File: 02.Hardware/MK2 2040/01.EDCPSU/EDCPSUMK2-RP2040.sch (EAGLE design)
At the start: 192 parts, among them IC1 W25Q64JVSSIQ, IC2 LM4040C25FTA, IC3 AP64501SP-13, J1 DX07S016JA1R1500, J2 RP2040TR7, J4 FTDI CONECTOR, J6 Display, K1 FLEX CONNECTORES, Q2 2N7002PW, Q4 2N7002PW, Q5 2N7002PW, Q9 2N7002PW, U10 IP2721, U2 MCP4725, U3 SN74AC14PWR, U4 MAX9938FEUK+T, U6 SN74AC14PWR, U7 TPIC2810D, U9 MAX9064EUK+T, Y1 ABLS-12.000MHZ-B4-T

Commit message: correccion esquamtico
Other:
- note added: "3v3 DCDC Buck"
- note removed: "3v3 LDO/DCDC Buck"
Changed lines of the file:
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@@
 Fc= 7Hz</text>
 <text x="-474.98" y="198.12" size="6.4516" layer="94">SWD PROGRAMMER CONNECTOR</text>
-<text x="-462.28" y="106.68" size="6.4516" layer="94">3v3 LDO/DCDC Buck</text>
+<text x="-462.28" y="106.68" size="6.4516" layer="94">3v3 DCDC Buck</text>
 <text x="-439.42" y="86.36" size="1.778" layer="91">OJO:
 Indicar en BOM que

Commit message: 1º Colocacion de componentes en el brd
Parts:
- removed R38: N.C, SparkFun-Resistors:RESISTOR0805
- removed TP1, TP10, TP11, TP12, TP14, TP4, TP6, TP7, TP9: M01POGOPIN_HOLE_LARGE, SparkFun-Connectors:M01POGOPIN_HOLE_LARGE
- removed TP2: VCCIO, SparkFun-Connectors:M01POGOPIN_HOLE_LARGE
- removed TP3: M01NOSILK-KIT, SparkFun-Connectors:M01NOSILK-KIT
- removed TP5: PEDAL, SparkFun-Connectors:M01POGOPIN_HOLE_LARGE
- added C65: N.C., SparkFun-Passives:CAP0805
- added JP1, JP2, JP5: JUMPER-SMT_2_NO_NO-SILK, SparkFun-Jumpers:JUMPER-SMT_2_NO_NO-SILK
- added R58, R60: N.C, SparkFun-Resistors:RESISTOR0805
- C45, C46: device SparkFun-Passives:CAP1206 -> SparkFun-Passives:CAP0805
- Y1: value ABLS-12.000MHZ-B4-T -> ABM3C-12.000MHZ-D4Y-T; device ABLS-12.000MHZ-B4-T:ABLS-12.000MHZ-B4-T -> ABM3C-12.000MHZ-D4Y-T:ABM3C-12.000MHZ-D4Y-T
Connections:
- net SPARE renamed PDL
- removed net IN+1: D1.2
- removed net SPARE2: R38.1
- removed net VCC-ISO: C1.2, C12.2, C15.1, C16.2, C2.2, C20.2, C25.2, C26.1, C3.2, C31.2, C44.2, C45.1, C5.2, C50.2, C51.2, C52.2, C53.2, C57.1, C6.2, C60.2, C62.2, C7.2, C8.2, D2.C, D3.C, D7.C, IC1.VCC, J2.IOVDD_1, J2.IOVDD_2, J2.IOVDD_3, J2.IOVDD_4, J2.IOVDD_5, J2.IOVDD_6, J2.USB_VDD, J2.VREG_VIN, J4.VCC, J6.VCC, K1.P$4, L1.2, LS1.DUMMY, R13.2, R15.1, R19.2, R35.1, R40.2, R52.2, R53.2, R54.2, R57.2, R66.1, U2.VDD, U3P.VCC, U6P.VCC, U7.VCC, U9.VCC, Z1.K
- removed net VCCIO: TP2.1
- new net 3V3MCU: C1.2, C12.2, C15.1, C16.2, C2.2, C20.2, C25.2, C26.1, C3.2, C31.2, C44.2, C45.1, C5.2, C50.2, C51.2, C52.2, C53.2, C57.1, C6.2, C60.2, C62.2, C7.2, C8.2, D2.C, D3.C, D7.C, IC1.VCC, J2.IOVDD_1, J2.IOVDD_2, J2.IOVDD_3, J2.IOVDD_4, J2.IOVDD_5, J2.IOVDD_6, J2.USB_VDD, J2.VREG_VIN, J4.VCC, J6.VCC, K1.P$4, L1.2, LS1.+, R13.2, R15.1, R19.2, R35.1, R40.2, R52.2, R53.2, R54.2, R57.2, R66.1, U2.VDD, U3P.VCC, U6P.VCC, U7.VCC, U9.VCC, Z1.K
- new net N$45: R58.2, U2.SCL
- new net N$48: R60.2, U2.SDA
- net FB: now also JP2.2; no longer C52.1, R15.2, R16.1
- net GND: now also C65.1, Y1.GND_1, Y1.GND_2; no longer D4.COMMON_CATHODE, TP12.1
- net GND_IN: now also D4.COMMON_CATHODE
- net IN+: now also D1.2
- net ISENSE: no longer TP4.1
- net N$19: now also C65.2
- net N$38: now also C52.1, JP2.1, R15.2, R16.1; no longer R38.2, TP1.1
- net N$63: now also Y1.CRYSTAL_2; no longer Y1.2
- net OVC_ALARM: no longer TP10.1
- net PEDAL: no longer TP5.1
- net PUSH: no longer TP9.1
- net SCL: now also R58.1; no longer TP7.1, U2.SCL
- net SDA: now also R60.1; no longer TP6.1, U2.SDA
- net USB_D+: now also JP5.2
- net USB_D-: now also JP1.2
- net USB_DM: now also JP1.1
- net USB_DP: now also JP5.1
- net VOSEN: no longer TP3.1
- net VOUT: no longer TP11.1
- net VO_TPS: no longer TP14.1
- net XIN: now also Y1.CRYSTAL_1; no longer Y1.1
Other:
- moved on the sheet: C59, C61, R30, R46

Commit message: Pequeños cambios
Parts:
- added C66: 100n 50v X7R/X5R, SparkFun-Passives:CAP0805
- renumbered IC1 to U5, IC2 to U8, IC3 to U12, J2 to U1, PS1 to U11, Y1 to X1, Z1 to DZ1
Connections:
- net VCCA renamed 1V1MCU
- new net VCC-ISO: C6.2, U1.IOVDD_2
- net 2V5_REF: now also C66.2
- net 3V3MCU: no longer C6.2, U1.IOVDD_2
- net GND: now also C66.1
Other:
- note added: "EDCPSU MK2-RP2040 March-2023"
- note removed: "EDCPSU MK2r1 May-2022"
- moved on the sheet: C5, R57

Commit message: Continuacion de cambios. Rutado inicial de todos los componentes. Falta asignacion de pines.
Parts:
- removed C1: 100n 50v X7R/X5R, SparkFun-Passives:CAP0805
- removed IN-: TEST-POINT3, SparkFun-Connectors:TEST-POINT3
- removed J4: FTDI CONECTOR, SparkFun-Connectors:FTDI_DEVICE
- added R38: 27R, SparkFun-Resistors:RESISTOR0805
- added R63: R27, SparkFun-Resistors:RESISTOR0805
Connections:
- removed net DTR: J4.DTR
- removed net RX-I: J4.RXI
- removed net TX-O: J4.TXO
- removed net VCC-ISO: C6.2, U1.IOVDD_2
- new net N$64: JP5.1, R38.1
- new net N$65: JP1.1, R63.1
- net 3V3MCU: now also C6.2, U1.IOVDD_2; no longer C1.2, J4.VCC
- net GND: no longer C1.1, D1.1, J4.CTS, J4.GND
- net GND_IN: now also D1.1; no longer IN-.1
- net USB_DM: now also R63.2; no longer JP1.1
- net USB_DP: now also R38.2; no longer JP5.1
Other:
- moved on the sheet: C16, C32, C50, C7, JP1, JP5

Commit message: Pequeñas modificaciones
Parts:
- R63: value R27 -> 27R
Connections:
- new net VCC-ISO: C15.1, C8.2, U5.VCC
- net 3V3MCU: no longer C15.1, C8.2, U5.VCC
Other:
- note added: "TVS ESD Protection Data"
- moved on the sheet: C15, C57, C8, D1, J1, R55, R56

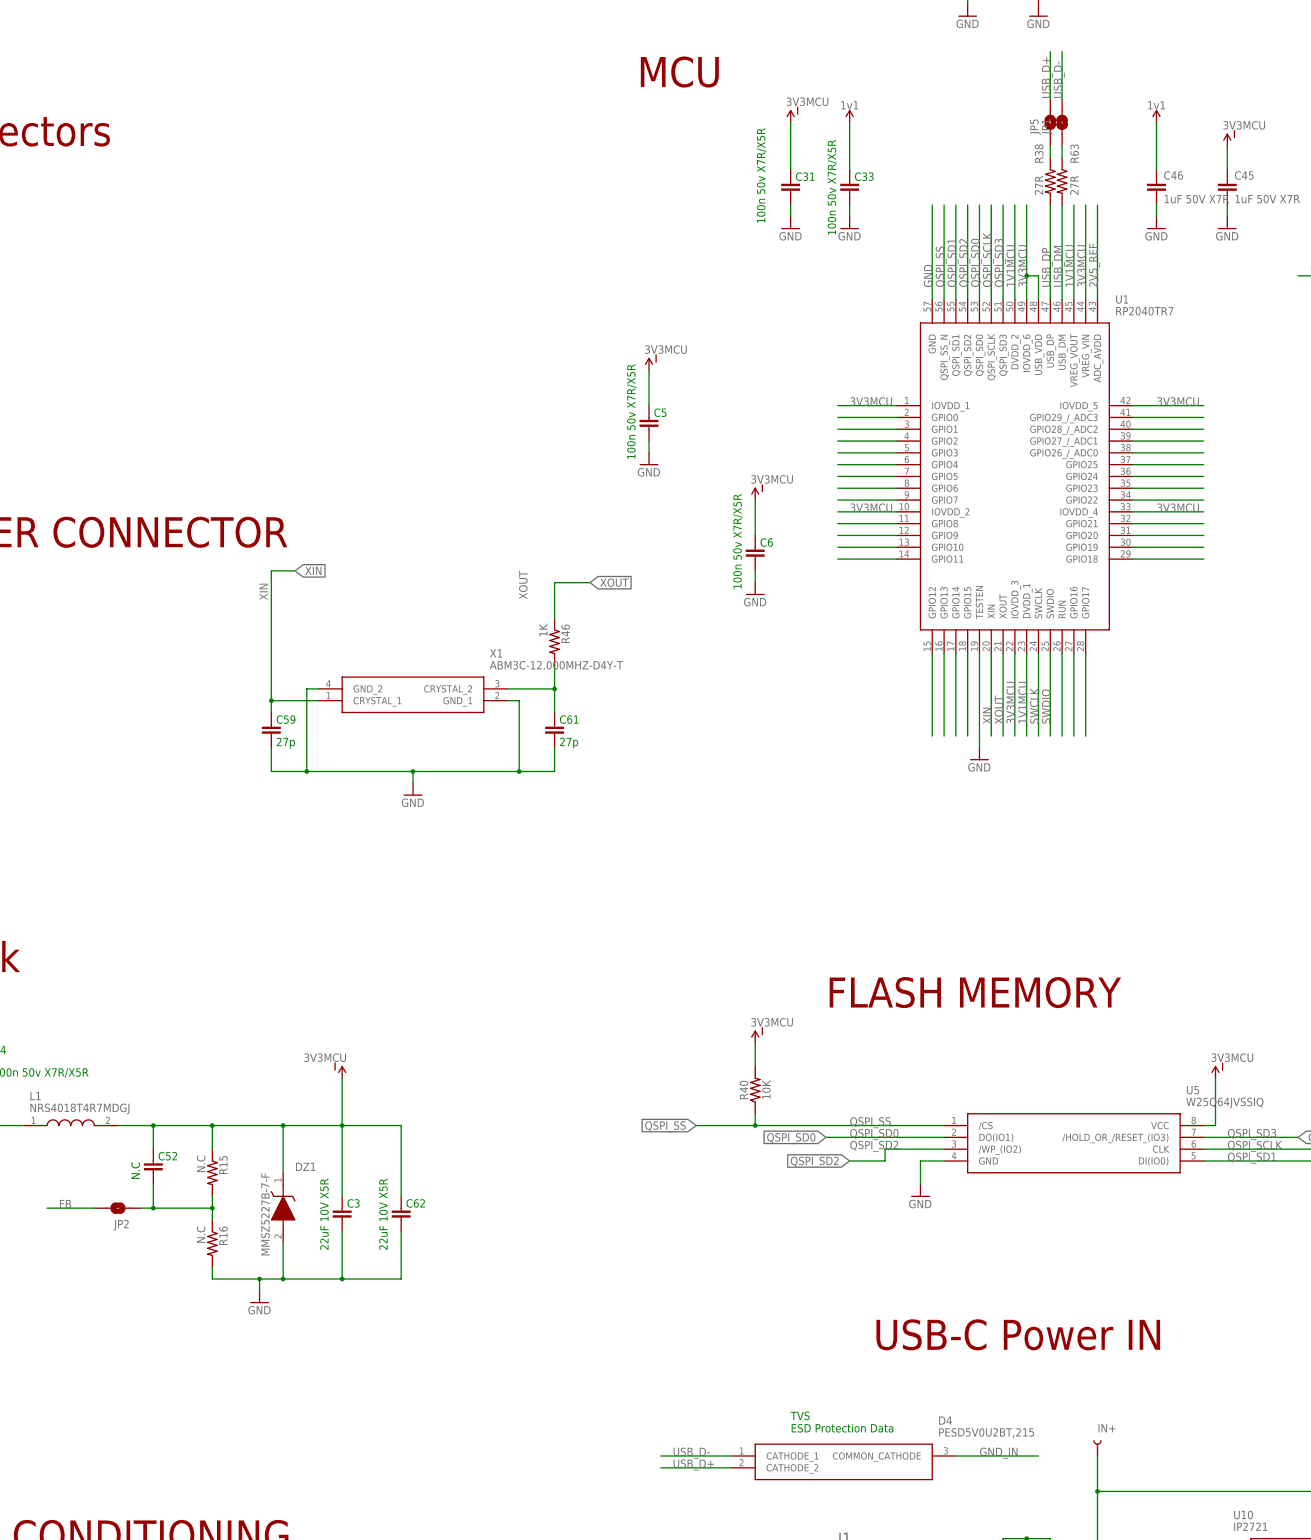
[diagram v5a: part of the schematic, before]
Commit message: Propuesta de routeado 1
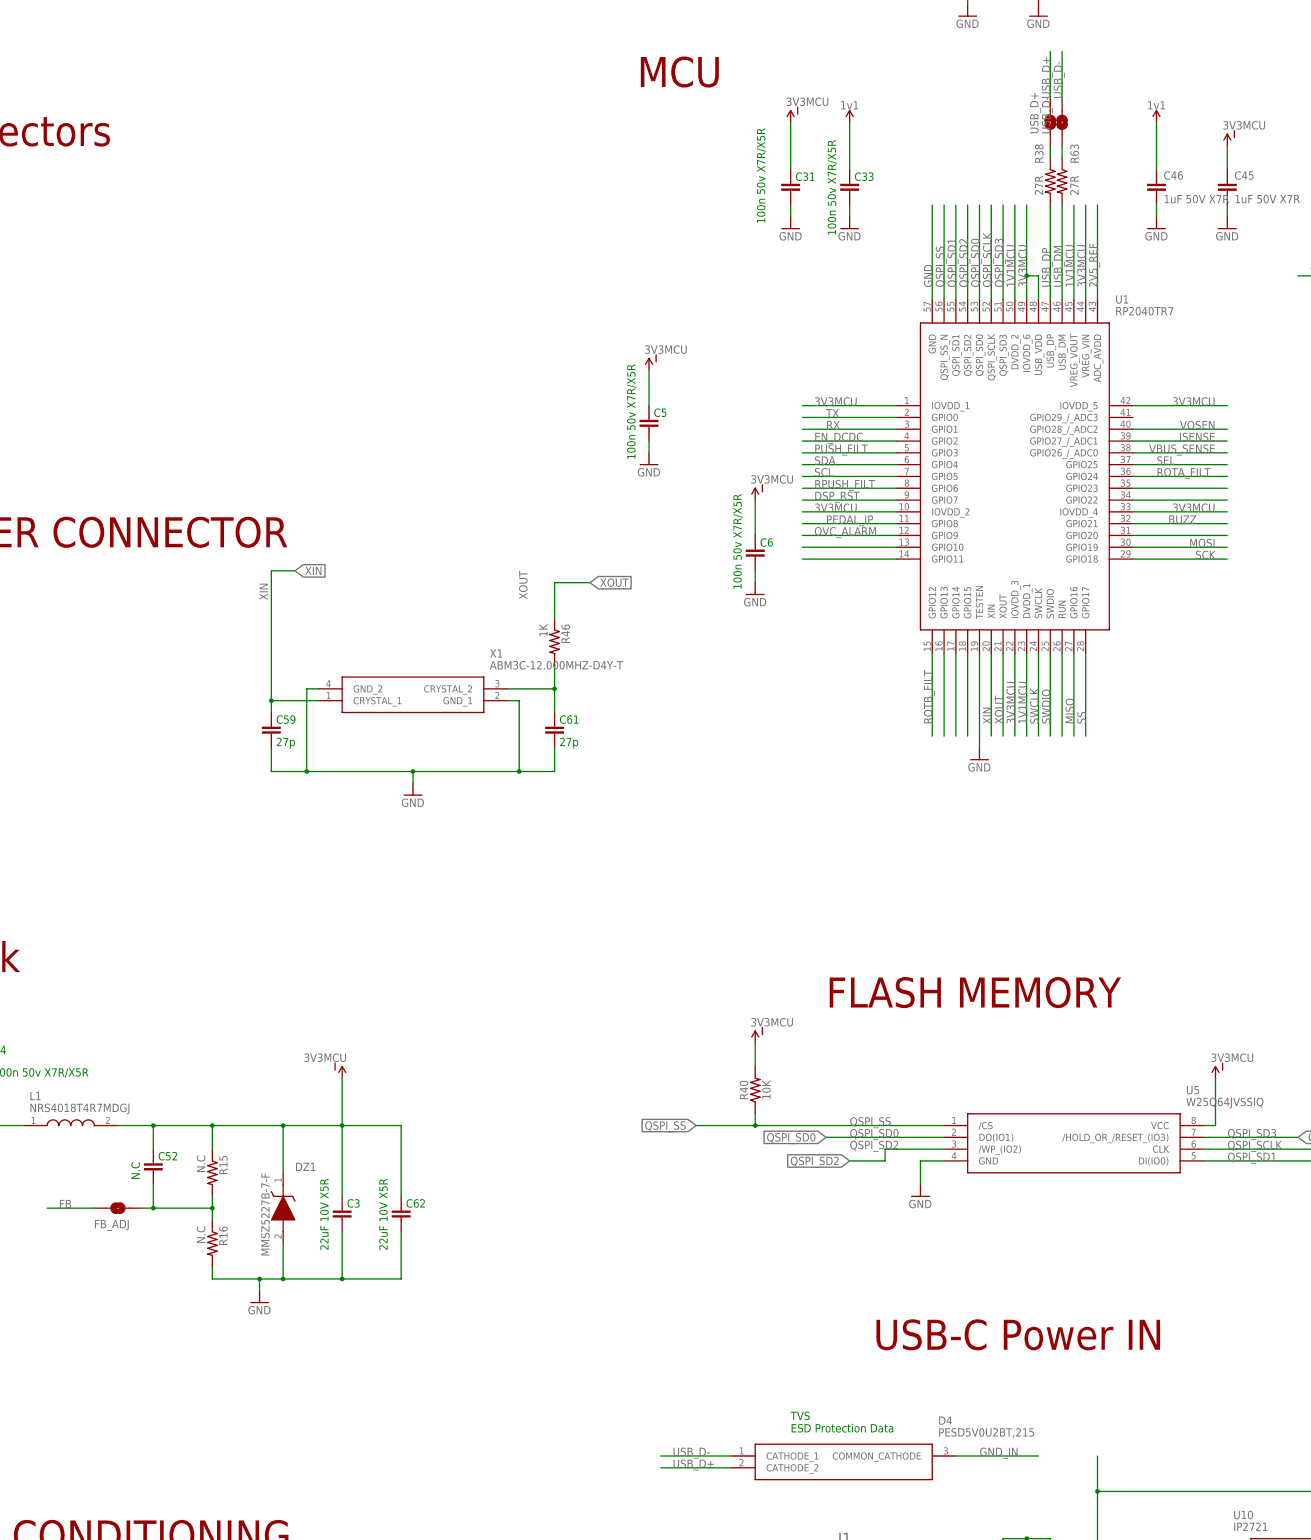
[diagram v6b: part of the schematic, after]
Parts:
- removed IN+: TEST-POINT3, SparkFun-Connectors:TEST-POINT3
- renumbered JP1 to USB_D-, JP2 to FB_ADJ, JP5 to USB_D+
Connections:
- net N$72 renamed TX
- net N$73 renamed RX
- removed net N$24: U1.GPIO29_/_ADC3
- removed net N$27: U1.GPIO28_/_ADC2
- removed net N$30: U1.GPIO25
- removed net N$33: U1.GPIO27_/_ADC1
- removed net N$36: U1.GPIO26_/_ADC0
- removed net N$42: U1.GPIO24
- removed net N$57: U1.GPIO21
- removed net N$61: U1.GPIO19
- removed net N$62: U1.GPIO18
- removed net N$74: U1.GPIO2
- removed net N$75: U1.GPIO3
- removed net N$76: U1.GPIO4
- removed net N$77: U1.GPIO5
- removed net N$78: U1.GPIO6
- removed net N$79: U1.GPIO7
- removed net N$80: U1.GPIO8
- removed net N$81: U1.GPIO9
- removed net N$84: U1.GPIO12
- removed net N$88: U1.GPIO17
- removed net N$89: U1.GPIO16
- net BUZZ: now also U1.GPIO21
- net DSP_RST: now also U1.GPIO7
- net EN_DCDC: now also U1.GPIO2
- net IN+: no longer IN+.1
- net ISENSE: now also U1.GPIO27_/_ADC1
- net MISO: now also U1.GPIO16
- net MOSI: now also U1.GPIO19
- net OVC_ALARM: now also U1.GPIO9
- net PEDAL_IP: now also U1.GPIO8
- net PUSH_FILT: now also U1.GPIO3
- net ROTA_FILT: now also U1.GPIO24
- net ROTB_FILT: now also U1.GPIO12
- net RPUSH_FILT: now also U1.GPIO6
- net SCK: now also U1.GPIO18
- net SCL: now also U1.GPIO5
- net SDA: now also U1.GPIO4
- net SEL: now also U1.GPIO25
- net SS: now also U1.GPIO17
- net VBUS_SENSE: now also U1.GPIO26_/_ADC0
- net VOSEN: now also U1.GPIO28_/_ADC2

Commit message: Propuesta de routeado 2
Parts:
- added JP1: 20021521-00010T1LF, 20021521-00010T1LF:20021521-00010T1LF
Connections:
- removed net N$100: U1.RUN
- new net RUN: JP1.10, U1.RUN
- new net SWO: JP1.6
- new net TDI: JP1.8
- net 3V3MCU: now also JP1.1
- net GND: now also JP1.3, JP1.5, JP1.7, JP1.9
- net SWCLK: now also JP1.4
- net SWDIO: now also JP1.2
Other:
- note added: "MK2-RP2040 v1-March-2023"
- note removed: "EDCPSU MK2-RP2040 March-2023"
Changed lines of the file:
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@@
 <part name="R63" library="SparkFun-Resistors" library_urn="urn:adsk.eagle:library:532" deviceset="RESISTOR" device="0805" package3d_urn="urn:adsk.eagle:package:39651/1" value="27R"/>
 <part name="U$7" library="SparkFun-Aesthetics" deviceset="VCC-ISO" device="" value="3V3MCU"/>
+<part name="JP1" library="20021521-00010T1LF" deviceset="20021521-00010T1LF" device=""/>
 </parts>
 <sheets>
@@
 <text x="-439.42" y="-17.78" size="6.4516" layer="94">SENSING CONDITIONING</text>
 <text x="-462.28" y="386.08" size="6.4516" layer="94">DIGITAL LDO + ROUTING + ISENSING</text>
-<text x="-320.04" y="429.26" size="6.4516" layer="94">EDCPSU MK2-RP2040
-March-2023</text>
+<text x="-320.04" y="429.26" size="6.4516" layer="94">MK2-RP2040
+v1-March-2023</text>
 <text x="76.2" y="322.58" size="1.778" layer="94">(DATA/COMMAND)</text>
 <text x="-193.04" y="358.14" size="1.778" layer="91">Overlap buzzer assy concentric</text>
@@
 <attribute name="VALUE" x="-143.256" y="87.376" size="1.778" layer="96"/>
 </instance>
+<instance part="JP1" gate="A" x="-345.44" y="350.52" smashed="yes">
+<attribute name="NAME" x="-351.796759375" y="358.783790625" size="1.779890625" layer="95"/>
+<attribute name="VALUE" x="-351.79805" y="340.3471" size="1.780259375" layer="96"/>
+</instance>
 </instances>
 <busses>
@@
 <wire x1="-109.22" y1="243.84" x2="-109.22" y2="246.38" width="0.1524" layer="91"/>
 </segment>
+<segment>
+<pinref part="JP1" gate="A" pin="3"/>
+<wire x1="-347.98" y1="353.06" x2="-363.22" y2="353.06" width="0.1524" layer="91"/>
+<label x="-360.68" y="353.06" size="1.778" layer="95"/>
+</segment>
+<segment>
+<pinref part="JP1" gate="A" pin="5"/>
+<wire x1="-347.98" y1="350.52" x2="-363.22" y2="350.52" width="0.1524" layer="91"/>
+<label x="-360.68" y="350.52" size="1.778" layer="95"/>
+</segment>
+<segment>
+<pinref part="JP1" gate="A" pin="9"/>
+<wire x1="-347.98" y1="345.44" x2="-363.22" y2="345.44" width="0.1524" layer="91"/>
+<label x="-360.68" y="345.44" size="1.778" layer="95"/>
+</segment>
+<segment>
+<pinref part="JP1" gate="A" pin="7"/>
+<wire x1="-347.98" y1="347.98" x2="-363.22" y2="347.98" width="0.1524" layer="91"/>
+<label x="-360.68" y="347.98" size="1.778" layer="95"/>
+</segment>
 </net>
 <net name="N$20" class="0">
@@
 <wire x1="-139.7" y1="279.4" x2="-139.7" y2="284.48" width="0.1524" layer="91"/>
 </segment>
+<segment>
+<pinref part="JP1" gate="A" pin="1"/>
+<wire x1="-347.98" y1="355.6" x2="-363.22" y2="355.6" width="0.1524" layer="91"/>
+<label x="-360.68" y="355.6" size="1.778" layer="95"/>
+</segment>
 </net>
 <net name="D0" class="0">
@@
 <label x="-177.8" y="160.02" size="1.778" layer="95" rot="R90"/>
 </segment>
+<segment>
+<pinref part="JP1" gate="A" pin="2"/>
+<wire x1="-340.36" y1="355.6" x2="-325.12" y2="355.6" width="0.1524" layer="91"/>
+<label x="-335.28" y="355.6" size="1.778" layer="95"/>
+</segment>
 </net>
 <net name="SWCLK" class="0">
@@
 <label x="-180.34" y="160.02" size="1.778" layer="95" rot="R90"/>
 </segment>
+<segment>
+<pinref part="JP1" gate="A" pin="4"/>
+<wire x1="-340.36" y1="353.06" x2="-325.12" y2="353.06" width="0.1524" layer="91"/>
+<label x="-335.28" y="353.06" size="1.778" layer="95"/>
+</segment>
 </net>
 <net name="XOUT" class="0">
@@
 </segment>
 </net>
-<net name="N$100" class="0">
-<segment>
-<pinref part="U1" gate="G$1" pin="RUN"/>
-<wire x1="-175.26" y1="175.26" x2="-175.26" y2="157.48" width="0.1524" layer="91"/>
-</segment>
-</net>
 <net name="1V1MCU" class="0">
 <segment>
@@
 </segment>
 </net>
+<net name="SWO" class="0">
+<segment>
+<pinref part="JP1" gate="A" pin="6"/>
+<wire x1="-340.36" y1="350.52" x2="-325.12" y2="350.52" width="0.1524" layer="91"/>
+<label x="-335.28" y="350.52" size="1.778" layer="95"/>
+</segment>
+</net>
+<net name="TDI" class="0">
+<segment>
+<pinref part="JP1" gate="A" pin="8"/>
+<wire x1="-340.36" y1="347.98" x2="-325.12" y2="347.98" width="0.1524" layer="91"/>
+<label x="-335.28" y="347.98" size="1.778" layer="95"/>
+</segment>
+</net>
+<net name="RUN" class="0">
+<segment>
+<pinref part="JP1" gate="A" pin="10"/>
+<wire x1="-340.36" y1="345.44" x2="-325.12" y2="345.44" width="0.1524" layer="91"/>
+<label x="-335.28" y="345.44" size="1.778" layer="95"/>
+</segment>
+<segment>
+<pinref part="U1" gate="G$1" pin="RUN"/>
+<wire x1="-175.26" y1="175.26" x2="-175.26" y2="157.48" width="0.1524" layer="91"/>
+<label x="-175.26" y="160.02" size="1.778" layer="95" rot="R90"/>
+</segment>
+</net>

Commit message: Cambios menores antes de pedir a PCBWAY
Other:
- note added: "GND_IN es la masa original de entrada que se une al GND interno a traves de RSENSE DE 0.1R Toda la corriente de la EDCPSU pasa por RSENSE y se cierra en GND_IN de entrada. U9 registra la caida en RSENSE y si supera un valor predeterminado dispara el comparador que corta el ENABLE del DCDC. U9 esta referenciado a GND_IN para poder sensar la caida en RSENSE."
- note added: "Linea de corte en PCB"
- note added: "proteccion del bus de 3v3 con zener de 3v6"
- moved on the sheet: C16, C3, C35, C36, C50, C62, DZ1, PTC1, R59, U9
